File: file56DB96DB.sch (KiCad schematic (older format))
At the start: 2 parts, among them U1 MAX-M8

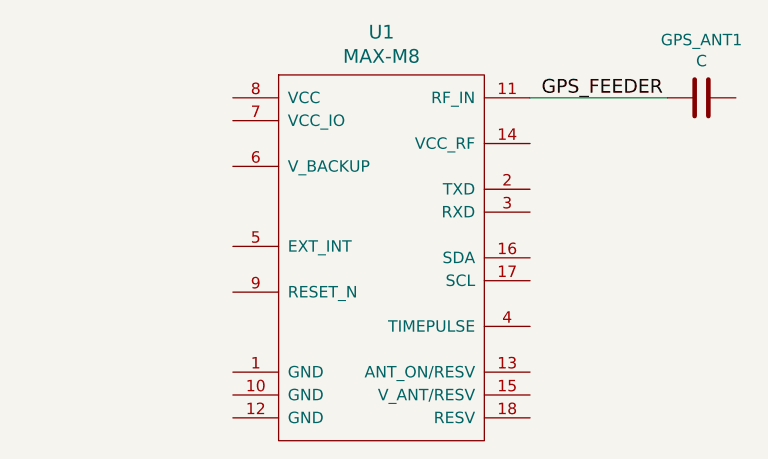
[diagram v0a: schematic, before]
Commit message: Added outline for AAA battery size
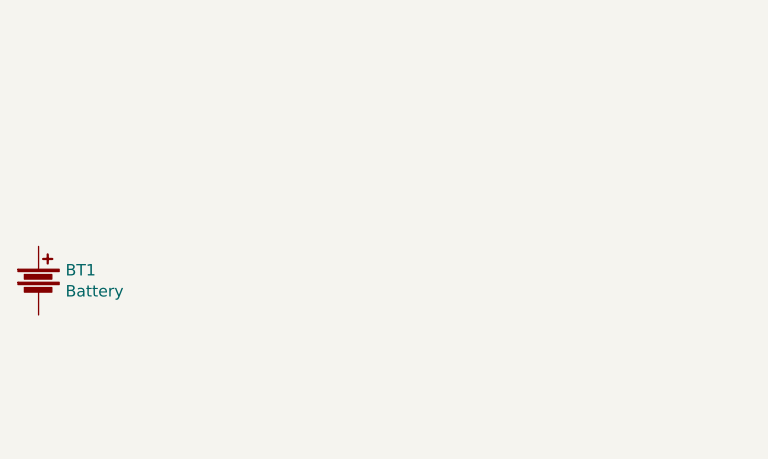
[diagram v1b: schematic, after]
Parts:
- removed GPS_ANT1: C, Capacitors_SMD:C_0603, symbol C
- removed U1: MAX-M8, _sensors:MAX-M8, symbol MAX-M8
- added BT1: Battery, symbol Battery
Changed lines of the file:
@@
 $Descr A4 11693 8268
 encoding utf-8
-Sheet 2 7
+Sheet 7 7
 Title ""
 Date ""
@@
 $EndDescr
 $Comp
-L MAX-M8 U1
-U 1 1 56DB59B1
-P 6100 2600
-F 0 "U1" H 6100 3237 60  0000 C CNN
-F 1 "MAX-M8" H 6100 3131 60  0000 C CNN
-F 2 "_sensors:MAX-M8" H 6950 3050 60  0001 C CNN
-F 3 "" H 6950 3050 60  0000 C CNN
-	1    6100 2600
+L Battery BT1
+U 1 1 56DB96F7
+P 4600 3050
+F 0 "BT1" H 4718 3096 50  0000 L CNN
+F 1 "Battery" H 4718 3004 50  0000 L CNN
+F 2 "" V 4600 3090 50  0000 C CNN
+F 3 "" V 4600 3090 50  0000 C CNN
+	1    4600 3050
 	1    0    0    -1
 $EndComp
-$Comp
-L C GPS_ANT1
-U 1 1 56DB5A9C
-P 7500 2250
-F 0 "GPS_ANT1" V 7247 2250 50  0000 C CNN
-F 1 "C" V 7339 2250 50  0000 C CNN
-F 2 "Capacitors_SMD:C_0603" H 7538 2100 50  0001 C CNN
-F 3 "" H 7500 2250 50  0000 C CNN
-F 4 "1575AT43A40" V 7500 2250 60  0001 C CNN "MPN"
-	1    7500 2250
-	0    1    1    0
-$EndComp
-Wire Wire Line
-	6750 2250 7350 2250
-Text Label 6800 2250 0    60   ~ 0
-GPS_FEEDER
 $EndSCHEMATC

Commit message: started layout, completed schematic
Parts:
- added C14, C17, C18: 10uF, symbol C_Small
- added C15, C16: 100nF, symbol C_Small
- added IC1: TPS61200, symbol TPS61200
- added L2: 2.2uH, symbol INDUCTOR_SMALL
- added R7: 2M, symbol R_Small
- added R8: 220K, symbol R_Small
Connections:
- net V_BAT: now reaches BT1.1
- net V_BAT: now also C14.1, C15.1, IC1.5 (VIN), IC1.6 (EN), IC1.8 (PS), L2.1, R7.1
- net GND: now reaches BT1.2
- net GND: now also C16.2, C17.2, C18.2, IC1.11 (PAD), IC1.12 (PAD), IC1.13 (PAD), IC1.14 (PAD), IC1.15 (PAD), IC1.4 (PGND), IC1.9 (GND), R8.2
- new net: C16.1, IC1.1 (VAUX)
- new net: C15.2, IC1.7 (UVLO), R7.2, R8.1
- new net: IC1.3 (L), L2.2
- new net +3V3: C17.1, C18.1, IC1.2 (VOUT)
- no-connect marks 0 -> 1
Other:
- moved on the sheet: BT1
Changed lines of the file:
@@
 LIBS:mpu-9250
 LIBS:SAMD21E17A
+LIBS:miniultrapro
+LIBS:texas-instruments
 LIBS:lorawan_gps-cache
 EELAYER 25 0
@@
 $Descr A4 11693 8268
 encoding utf-8
-Sheet 7 7
+Sheet 6 7
 Title ""
 Date ""
@@
 L Battery BT1
 U 1 1 56DB96F7
-P 4600 3050
-F 0 "BT1" H 4718 3096 50  0000 L CNN
-F 1 "Battery" H 4718 3004 50  0000 L CNN
-F 2 "" V 4600 3090 50  0000 C CNN
-F 3 "" V 4600 3090 50  0000 C CNN
-	1    4600 3050
-	1    0    0    -1
-$EndComp
+P 2400 3800
+F 0 "BT1" H 2518 3846 50  0000 L CNN
+F 1 "Battery" H 2518 3754 50  0000 L CNN
+F 2 "" V 2400 3840 50  0000 C CNN
+F 3 "" V 2400 3840 50  0000 C CNN
+	1    2400 3800
+	1    0    0    -1
+$EndComp
+$Comp
+L TPS61200 IC1
+U 1 1 56EB16DB
+P 4700 3750
+F 0 "IC1" H 4300 4350 50  0000 C CNN
+F 1 "TPS61200" H 4950 4350 50  0000 C CNN
+F 2 "" H 4700 3750 60  0000 C CNN
+F 3 "" H 4700 3750 60  0000 C CNN
+	1    4700 3750
+	1    0    0    -1
+$EndComp
+$Comp
+L GND #PWR29
+U 1 1 56EB0875
+P 4700 4750
+F 0 "#PWR29" H 4700 4500 50  0001 C CNN
+F 1 "GND" H 4700 4600 50  0000 C CNN
+F 2 "" H 4700 4750 50  0000 C CNN
+F 3 "" H 4700 4750 50  0000 C CNN
+	1    4700 4750
+	1    0    0    -1
+$EndComp
+$Comp
+L C_Small C16
+U 1 1 56EB090D
+P 5550 3950
+F 0 "C16" H 5560 4020 50  0000 L CNN
+F 1 "100nF" H 5560 3870 50  0000 L CNN
+F 2 "" H 5550 3950 50  0000 C CNN
+F 3 "" H 5550 3950 50  0000 C CNN
+	1    5550 3950
+	1    0    0    -1
+$EndComp
+$Comp
+L C_Small C18
+U 1 1 56EB0964
+P 6300 3950
+F 0 "C18" H 6310 4020 50  0000 L CNN
+F 1 "10uF" H 6310 3870 50  0000 L CNN
+F 2 "" H 6300 3950 50  0000 C CNN
+F 3 "" H 6300 3950 50  0000 C CNN
+	1    6300 3950
+	1    0    0    -1
+$EndComp
+$Comp
+L C_Small C15
+U 1 1 56EB09CB
+P 3150 3050
+F 0 "C15" H 3160 3120 50  0000 L CNN
+F 1 "100nF" H 3160 2970 50  0000 L CNN
+F 2 "" H 3150 3050 50  0000 C CNN
+F 3 "" H 3150 3050 50  0000 C CNN
+	1    3150 3050
+	1    0    0    -1
+$EndComp
+$Comp
+L C_Small C14
+U 1 1 56EB0A1E
+P 2900 3800
+F 0 "C14" H 2910 3870 50  0000 L CNN
+F 1 "10uF" H 2910 3720 50  0000 L CNN
+F 2 "" H 2900 3800 50  0000 C CNN
+F 3 "" H 2900 3800 50  0000 C CNN
+	1    2900 3800
+	1    0    0    -1
+$EndComp
+$Comp
+L INDUCTOR_SMALL L2
+U 1 1 56EB0AAB
+P 4700 2800
+F 0 "L2" H 4700 2900 50  0000 C CNN
+F 1 "2.2uH" H 4700 2750 50  0000 C CNN
+F 2 "" H 4700 2800 50  0000 C CNN
+F 3 "" H 4700 2800 50  0000 C CNN
+	1    4700 2800
+	1    0    0    -1
+$EndComp
+$Comp
+L R_Small R7
+U 1 1 56EB0AF6
+P 3550 3200
+F 0 "R7" H 3580 3220 50  0000 L CNN
+F 1 "2M" H 3580 3160 50  0000 L CNN
+F 2 "" H 3550 3200 50  0000 C CNN
+F 3 "" H 3550 3200 50  0000 C CNN
+	1    3550 3200
+	1    0    0    -1
+$EndComp
+$Comp
+L R_Small R8
+U 1 1 56EB0B5D
+P 3550 4000
+F 0 "R8" H 3580 4020 50  0000 L CNN
+F 1 "220K" H 3580 3960 50  0000 L CNN
+F 2 "" H 3550 4000 50  0000 C CNN
+F 3 "" H 3550 4000 50  0000 C CNN
+	1    3550 4000
+	1    0    0    -1
+$EndComp
+Wire Wire Line
+	4100 3800 4000 3800
+Wire Wire Line
+	4000 3800 4000 4550
+Wire Wire Line
+	5400 4550 5400 3800
+Wire Wire Line
+	5400 3800 5300 3800
+Wire Wire Line
+	5300 3700 5550 3700
+Wire Wire Line
+	5550 3700 5550 3850
+Wire Wire Line
+	5550 4550 5550 4050
+Connection ~ 5400 4550
+Wire Wire Line
+	4700 4450 4700 4750
+Connection ~ 4700 4550
+Wire Wire Line
+	4500 4550 4500 4450
+Connection ~ 4500 4550
+Wire Wire Line
+	4600 4550 4600 4450
+Connection ~ 4600 4550
+Wire Wire Line
+	4800 4550 4800 4450
+Connection ~ 4800 4550
+Wire Wire Line
+	4900 4550 4900 4450
+Connection ~ 4900 4550
+Connection ~ 6300 3500
+Connection ~ 5550 4550
+Connection ~ 4000 4550
+Wire Wire Line
+	4950 2800 5550 2800
+Wire Wire Line
+	5550 2800 5550 3400
+Wire Wire Line
+	5550 3400 5300 3400
+Wire Wire Line
+	4100 2800 4100 3700
+Connection ~ 4100 2800
+Wire Wire Line
+	2400 2800 2400 3650
+Wire Wire Line
+	3150 2950 3150 2800
+Connection ~ 3150 2800
+Wire Wire Line
+	3550 3300 3550 3900
+Wire Wire Line
+	3150 3600 4100 3600
+Connection ~ 3550 3600
+Wire Wire Line
+	3150 3150 3150 3600
+Wire Wire Line
+	3550 4100 3550 4550
+Wire Wire Line
+	2400 3950 2400 4550
+Connection ~ 3550 4550
+$Comp
+L +3V3 #PWR30
+U 1 1 56EB2DD1
+P 6650 3250
+F 0 "#PWR30" H 6650 3100 50  0001 C CNN
+F 1 "+3V3" H 6650 3390 50  0000 C CNN
+F 2 "" H 6650 3250 50  0000 C CNN
+F 3 "" H 6650 3250 50  0000 C CNN
+	1    6650 3250
+	1    0    0    -1
+$EndComp
+Wire Wire Line
+	5300 3500 6650 3500
+Wire Wire Line
+	6650 3500 6650 3250
+Text HLabel 2750 2450 2    60   Output ~ 0
+V_BAT
+Wire Wire Line
+	2750 2450 2550 2450
+Wire Wire Line
+	2550 2450 2550 2800
+Connection ~ 2550 2800
+NoConn ~ 5300 3600
+Wire Wire Line
+	2900 3700 2900 2800
+Connection ~ 2900 2800
+Wire Wire Line
+	2900 3900 2900 4550
+Wire Wire Line
+	2400 4550 6300 4550
+Connection ~ 4100 3400
+Connection ~ 4100 3500
+Wire Wire Line
+	2400 2800 4450 2800
+Wire Wire Line
+	3550 3100 3550 2800
+Connection ~ 3550 2800
+$Comp
+L C_Small C17
+U 1 1 56EC5227
+P 6050 3950
+F 0 "C17" H 6060 4020 50  0000 L CNN
+F 1 "10uF" H 6060 3870 50  0000 L CNN
+F 2 "" H 6050 3950 50  0000 C CNN
+F 3 "" H 6050 3950 50  0000 C CNN
+	1    6050 3950
+	1    0    0    -1
+$EndComp
+Wire Wire Line
+	6050 3500 6050 3850
+Connection ~ 6050 3500
+Wire Wire Line
+	6050 4050 6050 4550
+Connection ~ 6050 4550
+Wire Wire Line
+	6300 3500 6300 3850
+Wire Wire Line
+	6300 4550 6300 4050
 $EndSCHEMATC
